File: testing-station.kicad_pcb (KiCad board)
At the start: 4 copper layers, 212.7 x 113.3 mm, 97 parts, among them IC1 BME680, IC2 DS3231, IC3 74HC4050D, IC4 LP2985A, J1 pyranometer, J13 microSD, J2 anemometer, J3 AM2315C, J4 FPC connector, J5 Pt100, J7 Pt100, J9 Pt100, Q1 BSS138, SW1 500SSP1S2M2QEA, U1 TBA_1-0519, U2 MAX31865, U3 MIC5225, U4 MAX31865, U5 MIC5225, U6 MAX31865, U7 MIC5225, U8 AP2112K-3.3

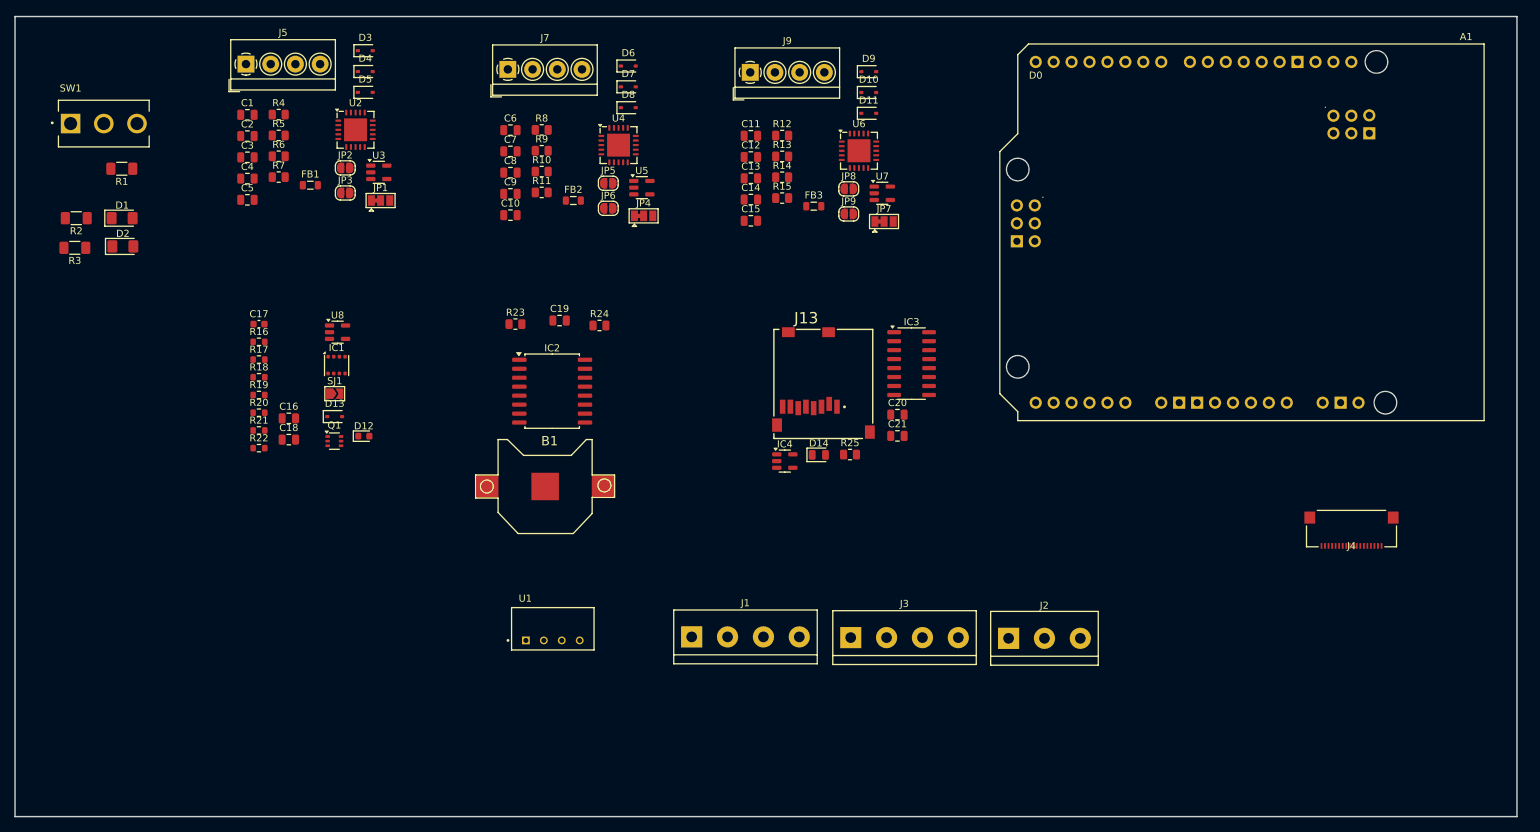
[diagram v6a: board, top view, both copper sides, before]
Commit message: changed to 2 layer board + created ground and +5V planes
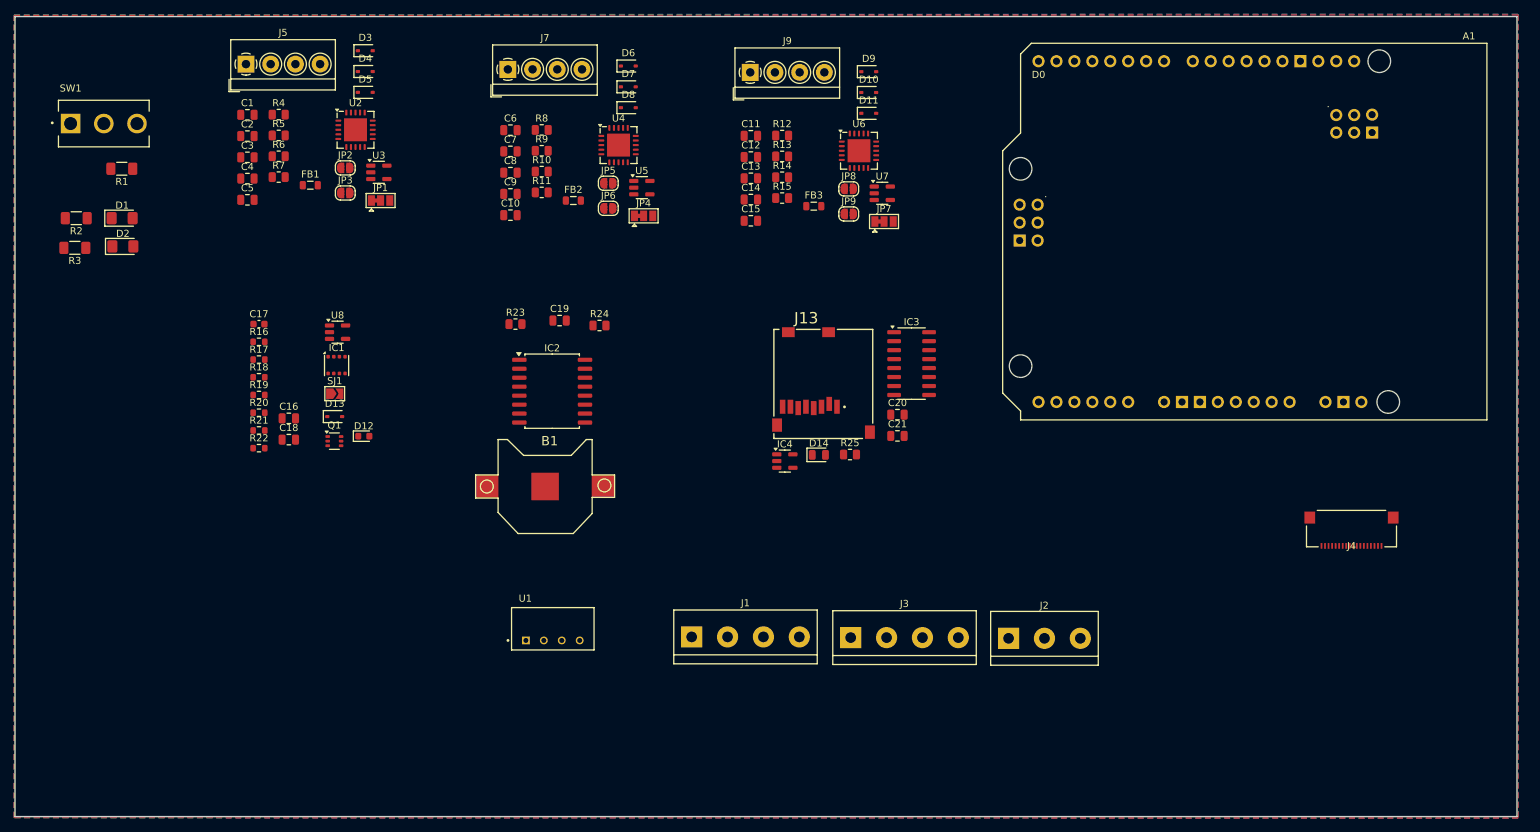
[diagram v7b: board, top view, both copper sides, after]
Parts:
- moved A1 0.41 mm to (250.1, 78.7)
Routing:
- added copper zone on F.Cu, net +5V
- added copper zone on B.Cu, net GND
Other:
- copper layers 4 -> 2
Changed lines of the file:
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@@
 	(paper "A4")
 	(layers
-		(0 "F.Cu" signal)
-		(1 "In1.Cu" signal)
-		(2 "In2.Cu" signal)
-		(31 "B.Cu" signal)
+		(0 "F.Cu" power)
+		(31 "B.Cu" power)
 		(32 "B.Adhes" user "B.Adhesive")
 		(33 "F.Adhes" user "F.Adhesive")
@@
 			)
 			(layer "dielectric 1"
-				(type "prepreg")
-				(color "FR4 natural")
-				(thickness 0.1)
-				(material "FR4")
-				(epsilon_r 4.5)
-				(loss_tangent 0.02)
-			)
-			(layer "In1.Cu"
-				(type "copper")
-				(thickness 0.035)
-			)
-			(layer "dielectric 2"
 				(type "core")
 				(color "FR4 natural")
-				(thickness 1.24)
-				(material "FR4")
-				(epsilon_r 4.5)
-				(loss_tangent 0.02)
-			)
-			(layer "In2.Cu"
-				(type "copper")
-				(thickness 0.035)
-			)
-			(layer "dielectric 3"
-				(type "prepreg")
-				(color "FR4 natural")
-				(thickness 0.1)
+				(thickness 1.51)
 				(material "FR4")
 				(epsilon_r 4.5)
@@
 	(footprint "PCM_arduino-library:Arduino_Uno_R4_WiFi_Shield"
 		(layer "B.Cu")
-		(at 249.680119 78.77 180)
+		(at 250.080119 78.67 180)
 		(descr "https://docs.arduino.cc/hardware/uno-r4-wifi")
 		(property "Reference" "A1"
@@
 		(layer "Edge.Cuts")
 	)
+	(zone
+		(net 108)
+		(net_name "+5V")
+		(layer "F.Cu")
+		(hatch edge 0.5)
+		(connect_pads
+			(clearance 0.5)
+		)
+		(min_thickness 0.25)
+		(filled_areas_thickness no)
+		(fill
+			(thermal_gap 0.5)
+			(thermal_bridge_width 0.5)
+		)
+		(polygon
+			(pts
+				(xy 41.5 21.4) (xy 254.5 21.3) (xy 254.5 135.062207) (xy 41.5 135)
+			)
+		)
+	)
+	(zone
+		(net 49)
+		(net_name "GND")
+		(layer "B.Cu")
+		(hatch edge 0.5)
+		(connect_pads
+			(clearance 0.5)
+		)
+		(min_thickness 0.25)
+		(filled_areas_thickness no)
+		(fill
+			(thermal_gap 0.5)
+			(thermal_bridge_width 0.5)
+		)
+		(polygon
+			(pts
+				(xy 41.5 21.3) (xy 254.5 21.2) (xy 254.5 135.1) (xy 41.5 135)
+			)
+		)
+	)
 )

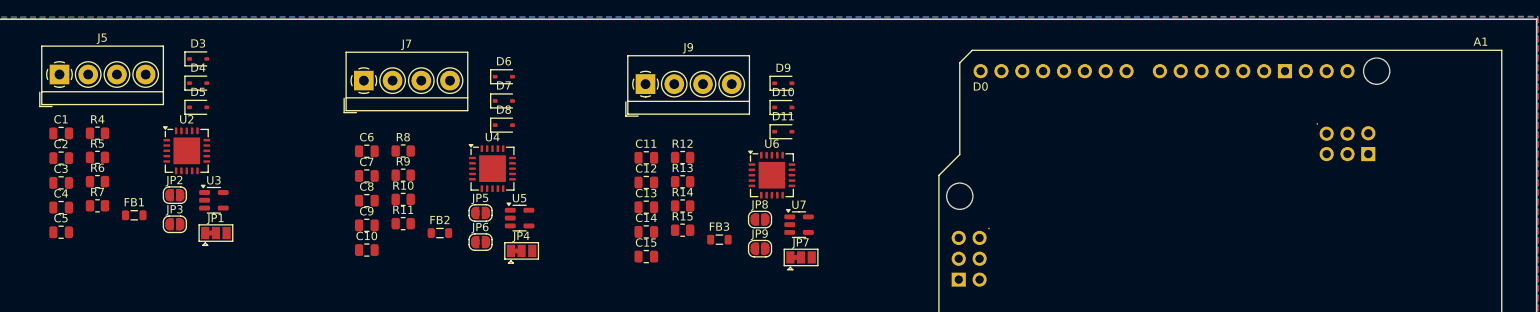
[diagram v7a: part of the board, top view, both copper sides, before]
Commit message: removed voltage regulators of each individual module
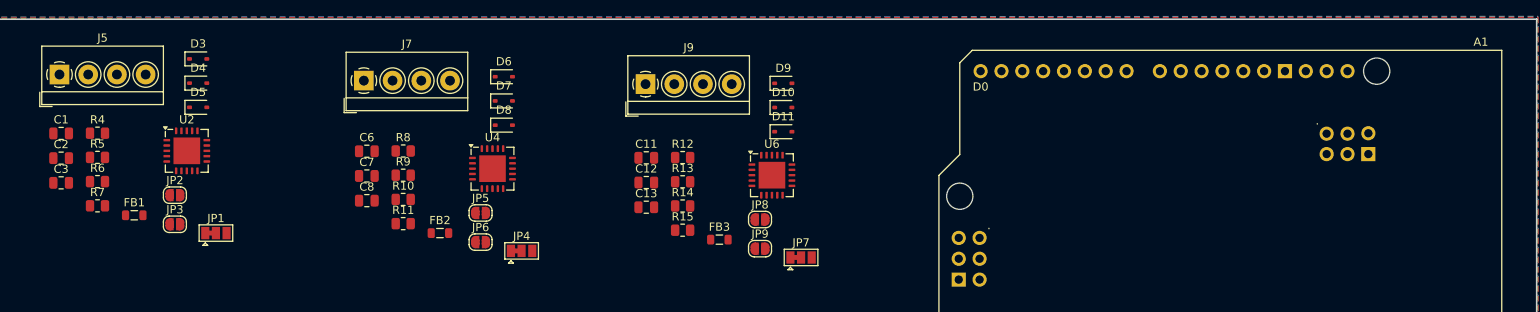
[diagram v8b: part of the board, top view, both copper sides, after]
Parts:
- removed C10, C14, C15, C4, C5, C9: 10uF, Capacitor_SMD:C_0805_2012Metric
- removed U3, U5, U7: MIC5225, Package_TO_SOT_SMD:SOT-23-5
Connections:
- C1 pad 1: VDD -> +3.3V
- C11 pad 1: VDD -> +3.3V
- C6 pad 1: VDD -> +3.3V
- FB1 pad 2: VDD -> +3.3V
- FB2 pad 2: VDD -> +3.3V
- FB3 pad 2: VDD -> +3.3V
- IC1 pad 6: 3.3V -> +3.3V
- IC1 pad 8: 3.3V -> +3.3V
- IC2 pad 2: 3.3V -> +3.3V
- Q1 pad 2: 3.3V -> +3.3V
- Q1 pad 5: 3.3V -> +3.3V
- R10 pad 2: VDD -> +3.3V
- R12 pad 2: VDD -> +3.3V
- R13 pad 2: VDD -> +3.3V
- R14 pad 2: VDD -> +3.3V
- R16 pad 1: 3.3V -> +3.3V
- R17 pad 1: VCC -> +5V
- R18 pad 1: VCC -> +5V
- R19 pad 1: 3.3V -> +3.3V
- R20 pad 1: 3.3V -> +3.3V
- R21 pad 2: 3.3V -> +3.3V
- R22 pad 2: 3.3V -> +3.3V
- R23 pad 1: 3.3V -> +3.3V
- R24 pad 1: 3.3V -> +3.3V
- R4 pad 2: VDD -> +3.3V
- R5 pad 2: VDD -> +3.3V
- R6 pad 2: VDD -> +3.3V
- R8 pad 2: VDD -> +3.3V
- R9 pad 2: VDD -> +3.3V
- U2 pad 19: VDD -> +3.3V
- U4 pad 19: VDD -> +3.3V
- U6 pad 19: VDD -> +3.3V
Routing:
- added copper zone on F.Cu, net +3.3V
- removed copper zone on F.Cu, net +5V
